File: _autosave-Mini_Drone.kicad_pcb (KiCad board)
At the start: 2 copper layers, 94.2 x 113.7 mm, 67 parts, among them J1 Conn_01x02, J3 Conn_01x02, J4 Conn_01x06, J7 Conn_01x11, J8 Conn_01x11, Q1 AO3400A, Q2 AO3400A, Q3 AO3400A, Q4 AO3400A, SW2 Tactile Switch 3x4x2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

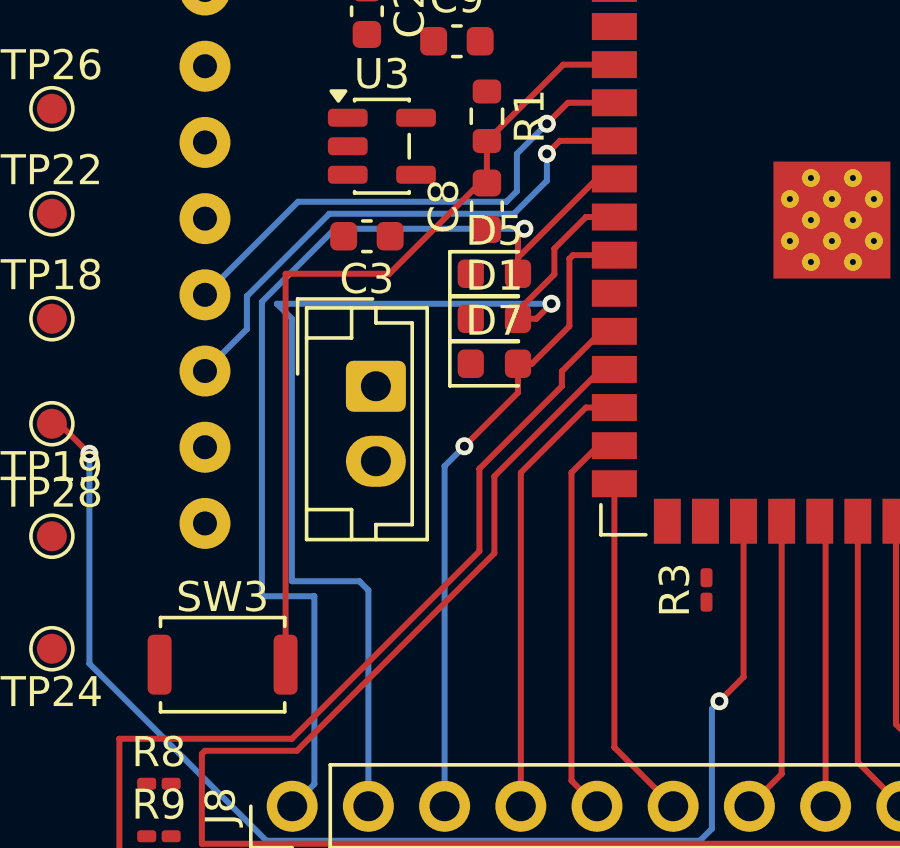
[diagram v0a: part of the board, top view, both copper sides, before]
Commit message: sch completed need add net classes and route
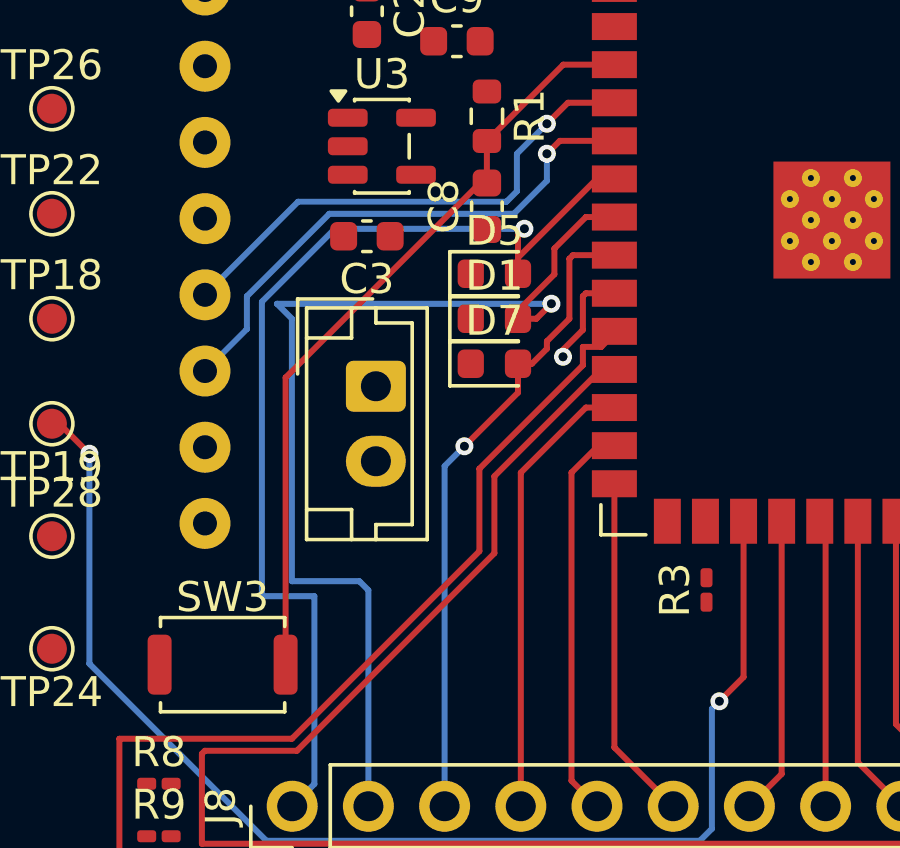
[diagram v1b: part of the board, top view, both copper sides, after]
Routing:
- net /M1: track 0.00 -> 3.38 mm, vias 0 -> 1
- net /EN: track 27.7 -> 25.7 mm
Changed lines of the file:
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@@
-	)
-	(segment
-		(start 201.29 82.75)
-		(end 204.75 82.75)
-		(width 0.2)
-		(layer "F.Cu")
-		(net 12)
 	)
 	(segment
@@
 	)
 	(segment
-		(start 204.75 82.75)
+		(start 201.29 86.21)
 		(end 207.775 79.725)
 		(width 0.2)
@@
 	(segment
 		(start 201.29 95.78)
-		(end 201.29 82.75)
+		(end 201.29 86.21)
 		(width 0.2)
 		(layer "F.Cu")
 		(net 12)
+	)
+	(segment
+		(start 212.25 84.75)
+		(end 212.25 84.67)
+		(width 0.2)
+		(layer "F.Cu")
+		(net 22)
+	)
+	(segment
+		(start 195.75 98.25)
+		(end 201.5 98.25)
+		(width 0.2)
+		(layer "F.Cu")
+		(net 22)
 	)
 	(segment
@@
 	)
 	(segment
+		(start 201.5 98.25)
+		(end 207.75 92)
+		(width 0.2)
+		(layer "F.Cu")
+		(net 22)
+	)
+	(segment
 		(start 207.75 92)
 		(end 207.75 89.25)
@@
 	)
 	(segment
+		(start 207.75 89.25)
+		(end 211.199 85.801)
+		(width 0.2)
+		(layer "F.Cu")
+		(net 22)
+	)
+	(segment
 		(start 237.25 102.25)
 		(end 195.75 102.25)
@@
 	)
 	(segment
-		(start 201.5 98.25)
-		(end 207.75 92)
-		(width 0.2)
-		(layer "F.Cu")
-		(net 22)
-	)
-	(segment
-		(start 211.83 84.67)
-		(end 212.25 84.67)
-		(width 0.2)
-		(layer "F.Cu")
-		(net 22)
-	)
-	(segment
-		(start 207.75 89.25)
-		(end 210.5 86.5)
-		(width 0.2)
-		(layer "F.Cu")
-		(net 22)
-	)
-	(segment
-		(start 210.5 86)
-		(end 211.83 84.67)
+		(start 211.199 85.189)
+		(end 211.811 85.189)
 		(width 0.2)
 		(layer "F.Cu")
@@
 	)
 	(segment
-		(start 195.75 98.25)
-		(end 201.5 98.25)
+		(start 211.811 85.189)
+		(end 212.25 84.75)
 		(width 0.2)
 		(layer "F.Cu")
@@
 	)
 	(segment
-		(start 210.5 86.5)
-		(end 210.5 86)
+		(start 211.199 85.801)
+		(end 211.199 85.189)
 		(width 0.2)
 		(layer "F.Cu")
@@
 	)
 	(segment
+		(start 210 85.25)
+		(end 210 85)
+		(width 0.2)
+		(layer "F.Cu")
+		(net 26)
+	)
+	(segment
+		(start 210.75 84.25)
+		(end 210.75 82.25)
+		(width 0.2)
+		(layer "F.Cu")
+		(net 26)
+	)
+	(segment
+		(start 210.75 82.25)
+		(end 210.87 82.13)
+		(width 0.2)
+		(layer "F.Cu")
+		(net 26)
+	)
+	(segment
 		(start 210.87 82.13)
 		(end 212.25 82.13)
@@
 	(segment
 		(start 209.0375 85.75)
+		(end 209.5 85.75)
+		(width 0.2)
+		(layer "F.Cu")
+		(net 26)
+	)
+	(segment
+		(start 209.0375 85.75)
 		(end 209.0375 86.7125)
 		(width 0.2)
@@
 	(segment
 		(start 209.5 85.75)
-		(end 210.75 84.5)
-		(width 0.2)
-		(layer "F.Cu")
-		(net 26)
-	)
-	(segment
-		(start 210.75 82.25)
-		(end 210.87 82.13)
-		(width 0.2)
-		(layer "F.Cu")
-		(net 26)
-	)
-	(segment
-		(start 209.0375 85.75)
-		(end 209.5 85.75)
+		(end 210 85.25)
+		(width 0.2)
+		(layer "F.Cu")
+		(net 26)
+	)
+	(segment
+		(start 210 85)
+		(end 210.75 84.25)
 		(width 0.2)
 		(layer "F.Cu")
@@
 		(start 209.0375 86.7125)
 		(end 207.25 88.5)
-		(width 0.2)
-		(layer "F.Cu")
-		(net 26)
-	)
-	(segment
-		(start 210.75 84.5)
-		(end 210.75 82.25)
 		(width 0.2)
 		(layer "F.Cu")
@@
 		(drill 0.3)
 		(layers "F.Cu" "B.Cu")
+		(tenting front back)
 		(net 27)
 	)
@@
 	)
 	(segment
+		(start 211.199 84.6219)
+		(end 210.536657 85.284243)
+		(width 0.2)
+		(layer "F.Cu")
+		(net 29)
+	)
+	(segment
+		(start 211.199 83.501)
+		(end 211.199 84.6219)
+		(width 0.2)
+		(layer "F.Cu")
+		(net 29)
+	)
+	(segment
+		(start 211.3 83.4)
+		(end 211.199 83.501)
+		(width 0.2)
+		(layer "F.Cu")
+		(net 29)
+	)
+	(segment
+		(start 210.536657 85.284243)
+		(end 210.536657 85.518329)
+		(width 0.2)
+		(layer "F.Cu")
+		(net 29)
+	)
+	(segment
+		(start 212.25 83.4)
+		(end 211.3 83.4)
+		(width 0.2)
+		(layer "F.Cu")
+		(net 29)
+	)
+	(via
+		(at 210.536657 85.518329)
+		(size 0.6)
+		(drill 0.3)
+		(layers "F.Cu" "B.Cu")
+		(net 29)
+	)
+	(segment
